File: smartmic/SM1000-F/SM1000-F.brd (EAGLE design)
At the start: 65 x 100 mm, 207 parts, among them CN1 HDR100-3, CN10 ST-3509, CN11 HDR100-3, CN12 HRS-A3C-16DA, CN2 JS-MU3-002, CN3 DS-0518, CN4 RJ-45, CN5 ST-3509, CN6 ST-3509, CN7 ST-3509, CN8 ST-3509, CN9 ST-3509, J1 JMP-2PIN, J2 JMP-2PIN, J3 JMP-2PIN, J4 CONN-BOOM-XH-2A, P1 TPAD50, P10 TPAD50, P11 TPAD50, P12 TPAD50, P13 TPAD50, P14 TPAD50, P16 TPAD50, P18 TPAD50, P19 TPAD50, P2 TPAD50, P20 TPAD50, P3 TPAD50, P4 TPAD50, P5 TPAD50, P6 TPAD50, P7 TPAD50, P8 TPAD50, P9 TPAD50, SW1 SW-LC2259, SW2 TS-026, SW3 SW-LC2259EENP, SW4 TS-026, SW5 TS-02B, T1 SM-LP-5001, T2 SM-LP-5001, U1 STM32F405VGT6, U2 LD3985M33R, U3 STMPS2141, U4 EMIF02-USB03F2, U5 TPS54329E, U6 LMV341, U7 LMV341, U8 LM386M-1, U9 LMV341

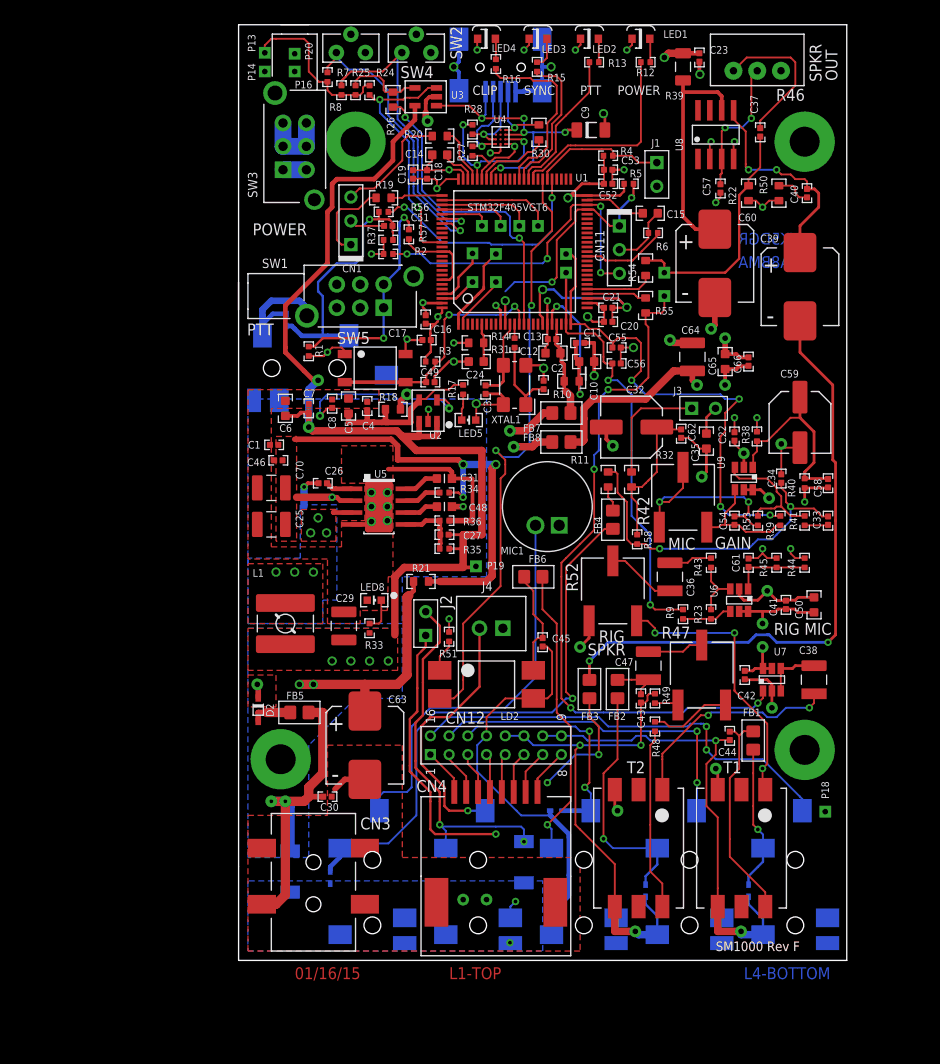
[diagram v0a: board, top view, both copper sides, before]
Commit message: Started implementing change-log items 34-41 RGB 09/15/15
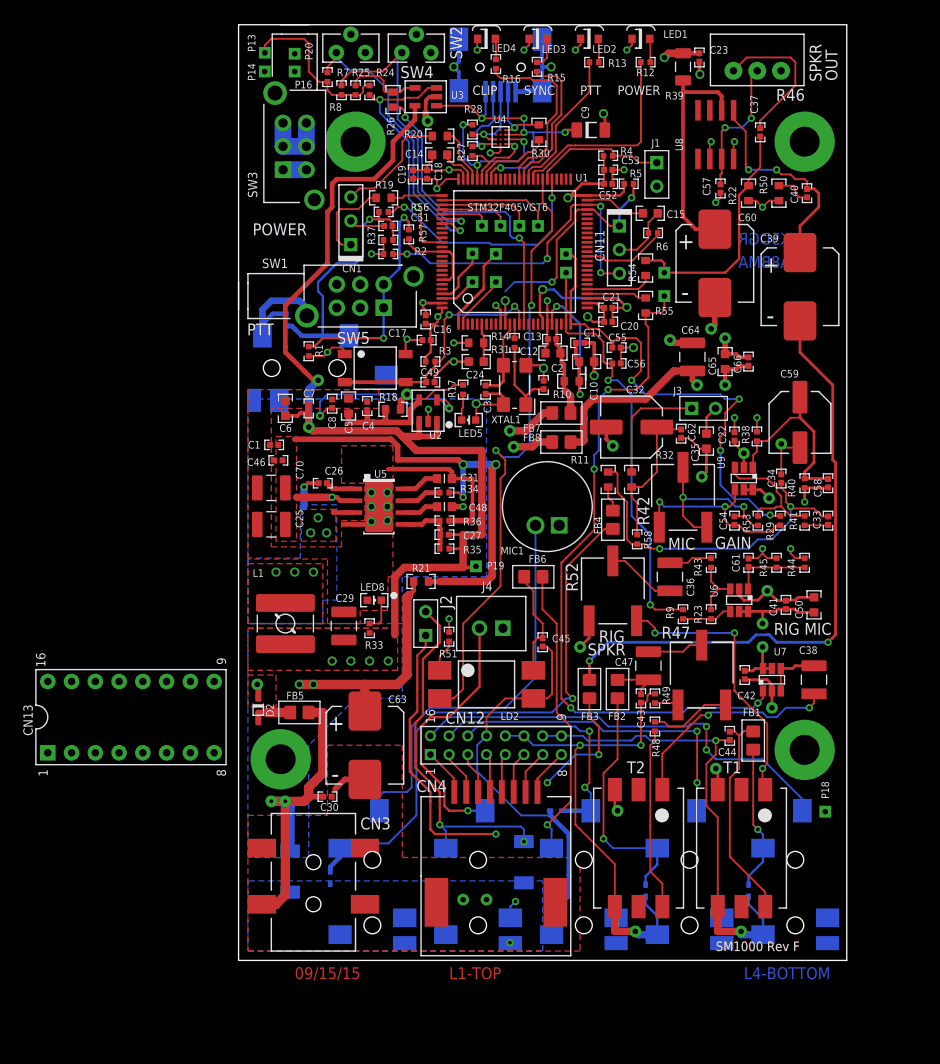
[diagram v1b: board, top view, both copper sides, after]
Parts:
- added CN13: DIL16X300, _RoweTel:DIL16X300
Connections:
- net N$27: now also R42.1; no longer R42.3
- net N$41: now also R42.3; no longer R42.1
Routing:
- net N$27: track 12.7 -> 20.6 mm, vias 0 -> 2
- net N$41: track 22.6 -> 19.1 mm
- net AIN2: track 53.6 -> 52.2 mm
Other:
- board text added: "09/15/15"
- board text removed: "01/16/15"

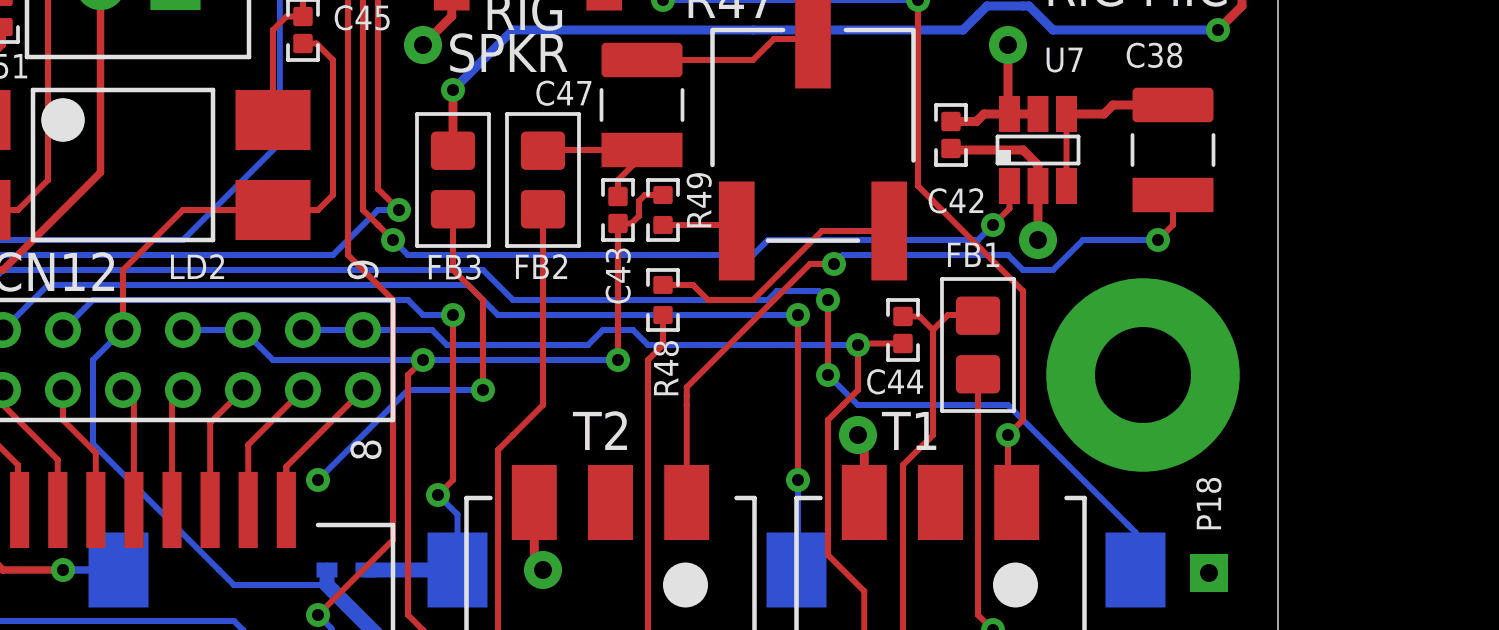
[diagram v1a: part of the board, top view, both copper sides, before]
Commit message: Show Schematic changes for CN12 pin swaps.  RGB 09/16/15
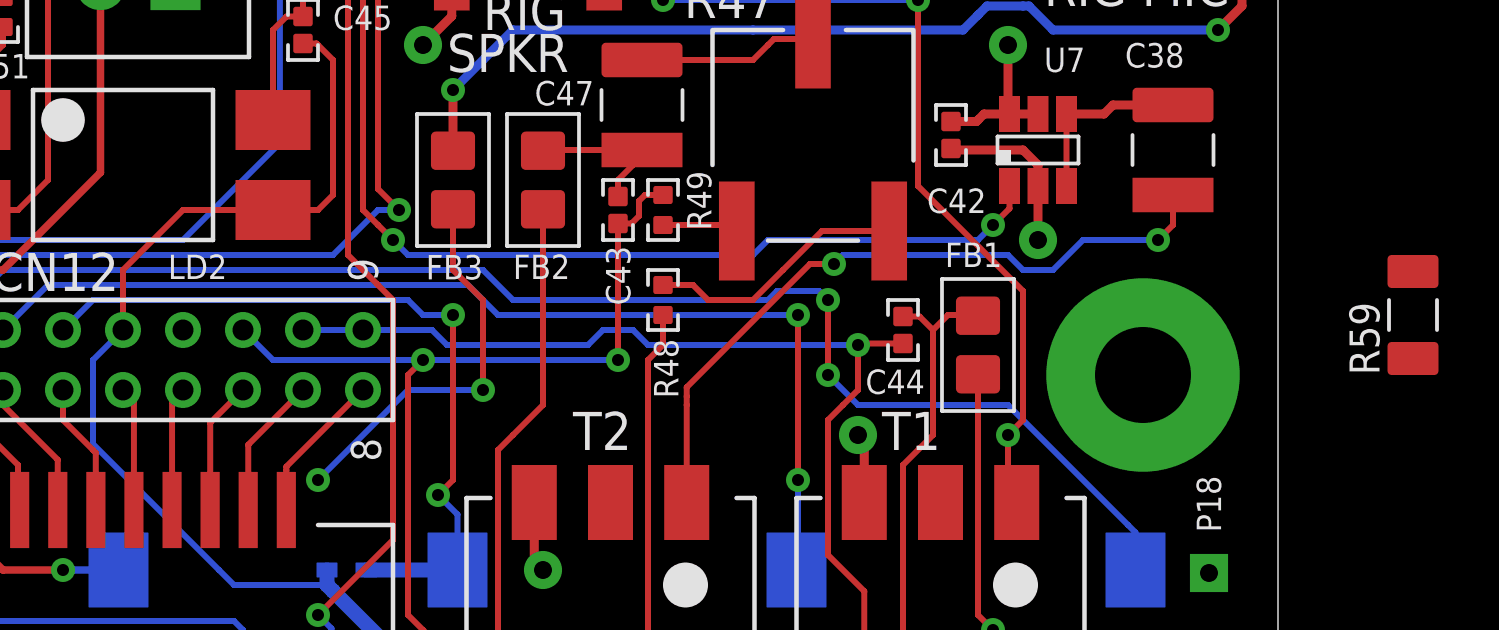
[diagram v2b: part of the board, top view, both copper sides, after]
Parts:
- added R59: (no value), AA-ipc-7351-resistor:RESC3115X70N
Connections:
- net RF_MIC: no longer CN12.12
- net RF_PTT: now also CN12.12
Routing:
- net RF_MIC: track 52.8 -> 50.8 mm
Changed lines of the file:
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@@
 <element name="DRILEGEND" library="drilegend" package="DRILEGEND" value="" x="21.266053125" y="-12.15666875"/>
 <element name="CN13" library="_RoweTel" package="DIL16X300" value="DIL16X300" x="-11.5" y="26"/>
+<element name="R59" library="AA-ipc-7351-resistor" package="RESC3115X70N" value="" x="69.5" y="24.5" rot="R90"/>
 </elements>
 <signals>
@@
 <contactref element="C43" pad="2"/>
 <contactref element="CN12" pad="11"/>
-<contactref element="CN12" pad="12"/>
 <wire x1="40.21" y1="10.29" x2="36.5" y2="14" width="0.2" layer="1"/>
 <wire x1="36.5" y1="14" x2="36" y2="14.5" width="0.2" layer="1"/>
 <wire x1="36" y1="22.5" x2="36.5" y2="23" width="0.2" layer="1"/>
 <via x="36.5" y="23" extent="1-16" drill="0.4" diameter="0.8"/>
-<wire x1="28.5" y1="24" x2="30.5" y2="24" width="0.2" layer="16"/>
 <wire x1="30.5" y1="24" x2="31.5" y2="23" width="0.2" layer="16"/>
 <wire x1="31.5" y1="23" x2="36.5" y2="23" width="0.2" layer="16"/>
@@
 <wire x1="32.5" y1="33.55" x2="32.95" y2="33.55" width="0.2" layer="1"/>
 <wire x1="32.95" y1="33.55" x2="33" y2="33.5" width="0.2" layer="1"/>
+<contactref element="CN12" pad="12"/>
+<wire x1="26.5" y1="24" x2="28.5" y2="24" width="0" layer="19" extent="1-1"/>
 </signal>
 <signal name="N$32">

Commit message: Update Schematic & board files. Add PDF of schematic for review. RGB
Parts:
- removed CN12: HRS-A3C-16DA, _RoweTel:HRS-A3C-16DA
- removed CN13: DIL16X300, _RoweTel:DIL16X300
- removed DRILEGEND: (no value), drilegend:DRILEGEND
- added CN112: DIL16X300, _RoweTel:DIL16X300
- added J5: JMP-2PIN, _Coherix:JMPR-2PIN
- added P15, P17, P21: TPAD50, _Coherix:TPAD50
- added R60: 330,1%, AA-ipc-7351-resistor:RESC3115X70N
- added R61, R62: (no value), AA-ipc-7351-resistor:RESC1608X55N
- added SH4: SHUNT,0.1IN, _Coherix:NOPACKAGE
- added U10: 24LC256-I/MS, coherix:MSOP-8
- R48: device AA-ipc-7351-resistor:RESC1005X40AN -> AA-ipc-7351-resistor:RESC3115X70N
- moved R59 31.3 mm to (65.0, -6.50)
- moved P19 7.27 mm to (18.5, 44.5)
- moved LD2 5.22 mm to (28.0, 34.5)
- moved J4 4.50 mm to (27.0, 40.0)
- moved R51 4.49 mm to (21.6, 39.0), turned to 0 degrees
- moved C45 3.61 mm to (35.5, 36.0)
- moved FB6 1.58 mm to (33.0, 40.5), turned to 270 degrees
- moved J2 1.00 mm to (20.0, 35.0)
- moved C27 0.50 mm to (21.5, 45.5)
- moved R35 0.50 mm to (21.5, 44.0)
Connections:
- new net N$75: J5.2, R60.1
- new net SCL3: R62.2, U1.41, U10.6
- new net SDA3: R61.2, U1.40, U10.5
- net APTT: now also CN112.14; no longer CN12.14
- net GND: now also P17.1, U10.1, U10.2, U10.3, U10.4, U10.7
- net MIC: now also CN112.15; no longer CN12.15
- net N$51: now also CN112.8, P15.1; no longer CN12.8
- net N$52: now also CN112.7; no longer CN12.7
- net N$53: now also CN112.6; no longer CN12.6
- net N$54: now also CN112.5; no longer CN12.5
- net N$55: now also CN112.4; no longer CN12.4
- net N$56: now also CN112.3; no longer CN12.3
- net N$57: now also CN112.2; no longer CN12.2
- net N$58: now also CN112.1; no longer CN12.1
- net N$77: now also P21.1
- net N$78: now also R60.2
- net N$82: now also J5.1
- net RF_MIC: now also CN112.11; no longer CN12.11
- net RF_PTT: now also CN112.12, CN112.13; no longer CN12.12, CN12.13
- net RF_SPKR: now also CN112.10, CN112.9; no longer CN12.10, CN12.9
- net SPKR: now also CN112.16; no longer CN12.16
- net VDD: now also R61.1, R62.1, U10.8
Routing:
- net N$76: track 60.7 -> 13.4 mm, vias 1 -> 0
- net N$60: track 43.6 -> 5.43 mm
- net N$62: track 70.8 -> 39.0 mm, vias 5 -> 3
- net SPKR: track 47.2 -> 18.4 mm
- net !CPPT!: track 65.0 -> 37.9 mm
- net RF_PTT: track 44.6 -> 18.9 mm
- net N$73: track 31.5 -> 6.22 mm
- net DAC1_OUT: track 74.1 -> 51.7 mm, vias 4 -> 3
- net N$72: track 28.4 -> 6.56 mm
- net APTT: track 25.6 -> 5.82 mm, vias 2 -> 1
- net N$64: track 39.6 -> 21.3 mm
- net MIC: track 36.1 -> 20.0 mm
- net RF_MIC: track 50.8 -> 37.5 mm, vias 3 -> 2
- net RF_SPKR: track 51.8 -> 42.1 mm
- net N$74: track 11.6 -> 2.67 mm
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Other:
- board text removed: "01-20"

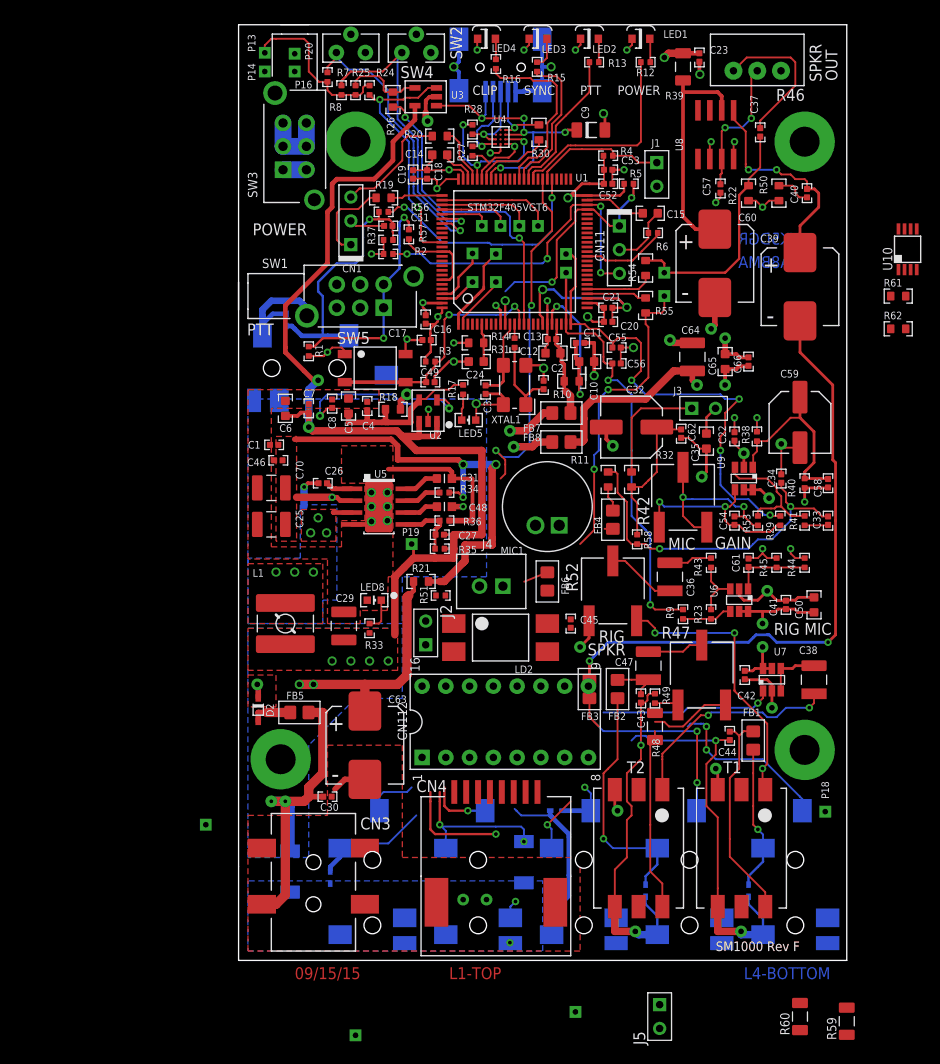
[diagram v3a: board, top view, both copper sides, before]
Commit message: ADD PDFs of Schematics and board layers L1, L2, L3 & L4 for reference only. RGB 10/03/15
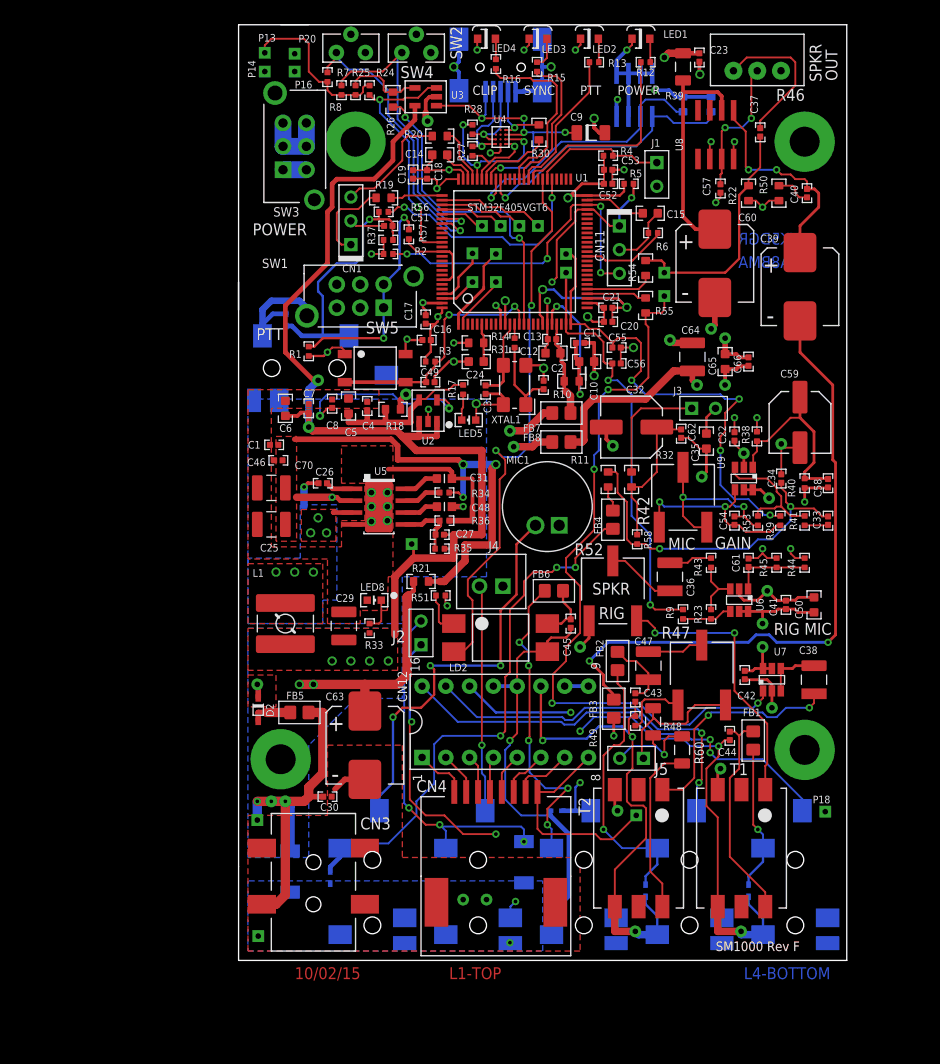
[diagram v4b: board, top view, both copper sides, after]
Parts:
- removed R59: (no value), AA-ipc-7351-resistor:RESC3115X70N
- added DRILEGEND: (no value), drilegend:DRILEGEND
- R61, R62: value (none) -> 4.7K,1%
- U10: device coherix:MSOP-8 -> _RoweTel:SOIC8
- moved U10 33.5 mm to (42.3, 92.5), flipped to the bottom, turned to 180 degrees
- moved R62 33.2 mm to (47.5, 91.5), flipped to the bottom, turned to 270 degrees
- moved R60 31.2 mm to (47.4, 22.5), turned to 270 degrees
- moved R61 28.6 mm to (50.5, 91.5), flipped to the bottom, turned to 270 degrees
- moved J5 27.8 mm to (42.0, 21.6), turned to 270 degrees
- moved P15 22.0 mm to (42.5, 15.5)
- moved P17 14.8 mm to (2.10, 2.60)
- moved P21 5.52 mm to (2.00, 15.0)
- moved FB3 3.34 mm to (40.1, 26.9)
- moved R49 3.19 mm to (42.4, 25.6)
- moved FB2 3.00 mm to (40.5, 32.0)
- moved FB6 1.22 mm to (33.7, 39.5), turned to 180 degrees
- moved SH4 1.12 mm to (5.50, -0.50)
- moved C43 0.61 mm to (42.4, 28.1)
- moved R48 0.54 mm to (44.3, 25.5)
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- renumbered CN112 to CN12
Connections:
- net SCL3: now also U1.67; no longer U1.41
- net SDA3: now also U1.66; no longer U1.40
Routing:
- net N$76: track 13.4 -> 58.3 mm, vias 0 -> 3
- net N$60: track 5.43 -> 43.3 mm, vias 0 -> 3
- net SPKR: track 18.4 -> 48.8 mm
- net SDA3: track 0.00 -> 29.9 mm, vias 0 -> 1
- net N$62: track 39.0 -> 68.3 mm, vias 3 -> 5
- net SCL3: track 0.00 -> 29.4 mm, vias 0 -> 1
- net RF_PTT: track 18.9 -> 46.5 mm, vias 0 -> 1
- net N$73: track 6.22 -> 33.4 mm, vias 1 -> 5
- net DAC1_OUT: track 51.7 -> 78.1 mm, vias 3 -> 4
- net N$51: track 0.00 -> 23.0 mm
- net !CPPT!: track 37.9 -> 59.5 mm
- net APTT: track 5.82 -> 26.1 mm, vias 1 -> 2
- net MIC: track 20.0 -> 39.1 mm
- net N$72: track 6.56 -> 24.2 mm
- net RF_MIC: track 37.5 -> 54.7 mm, vias 2 -> 3
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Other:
- board text added: "01-20"
- board text added: "10/02/15"
- board text removed: "09/15/15"
